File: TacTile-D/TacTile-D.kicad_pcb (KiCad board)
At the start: 2 copper layers, 59.9 x 59.9 mm, 19 parts, among them J1 Conn_01x06, J2 Conn_01x06, J3 Conn_01x06, J4 Conn_01x06, J5 Conn_01x04, J6 Conn_01x05, J7 Conn_01x02, J8 Conn_01x02, U1 74LVC2G08, U10 74LVC1G373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

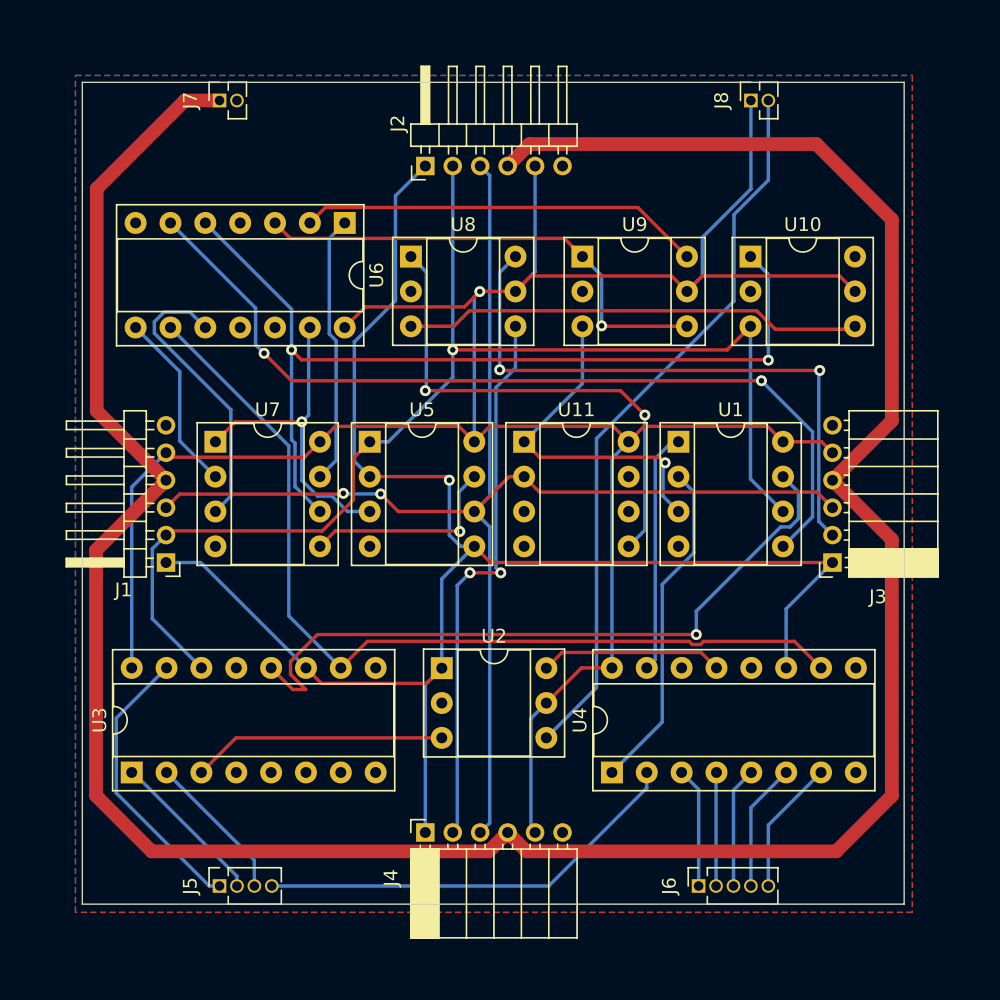
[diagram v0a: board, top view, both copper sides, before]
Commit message: Ensured outputs were disabled on reset - added not gate
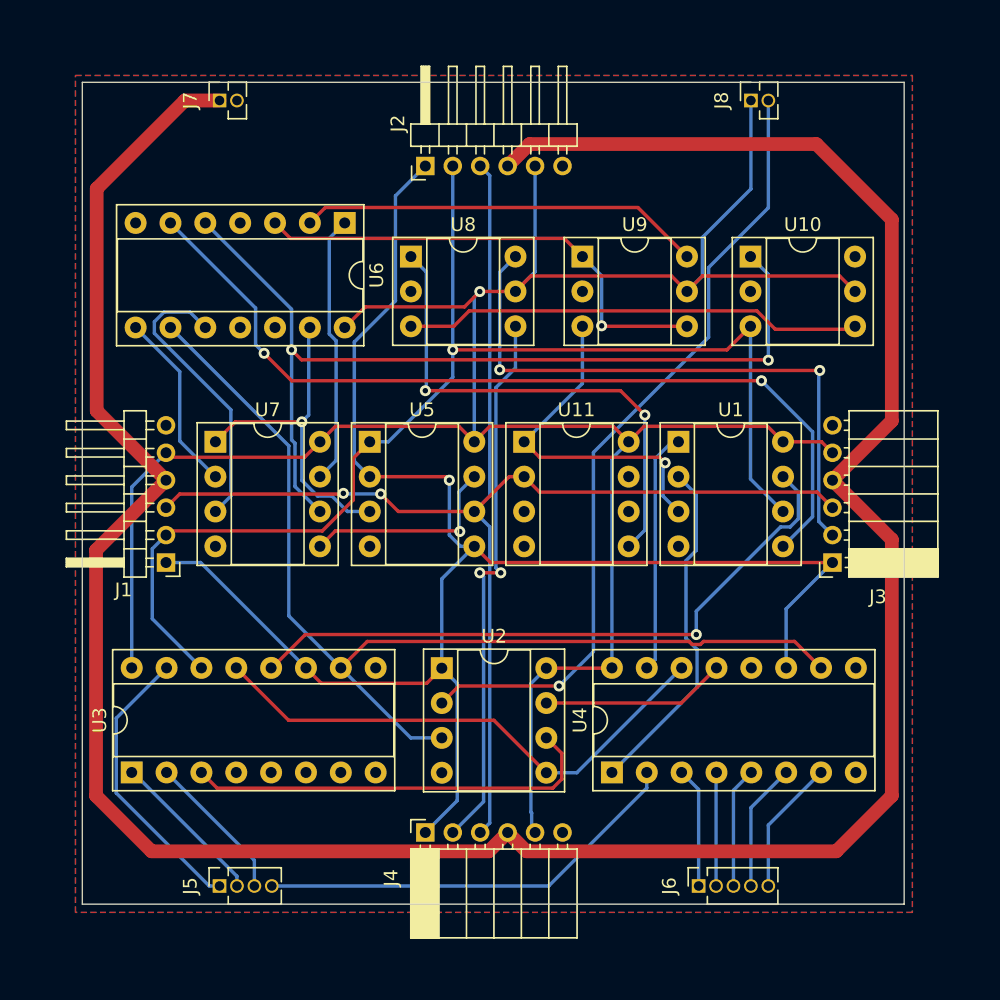
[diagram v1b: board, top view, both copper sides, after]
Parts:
- U2: value 74LVC2G04 -> 74LVC3G04; footprint Package_DIP:DIP-6_W7.62mm_Socket -> Package_DIP:DIP-8_W7.62mm_Socket
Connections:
- U2 pad 2: GND -> LEN
- U2 pad 3: Net-(U3-QD) -> SEN
- U2 pad 4: LEN -> GND
- U2 pad 5: VCC -> Net-(U3-~{OE})
- U2 pad 6: Net-(U4-CPR) -> Net-(U3-QD)
- U3 pad 13: GND -> Net-(U3-~{OE})
- U4 pad 14: GND -> Net-(U3-~{OE})
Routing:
- net Net-(U3-~{OE}): track 0.00 -> 38.8 mm
- net Net-(U3-QD): track 18.6 -> 30.5 mm
- net SEN: track 66.7 -> 76.2 mm
- net LEN: track 53.2 -> 58.1 mm, vias 0 -> 1
- net Net-(U3-RCLK): track 51.5 -> 47.5 mm
- net VCC: track 178.7 -> 180.2 mm
- net CLK: track 119.5 -> 120.5 mm
- net Net-(U4-Q1): track 24.5 -> 25.3 mm

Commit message: Mounted ICs without sockets to save space
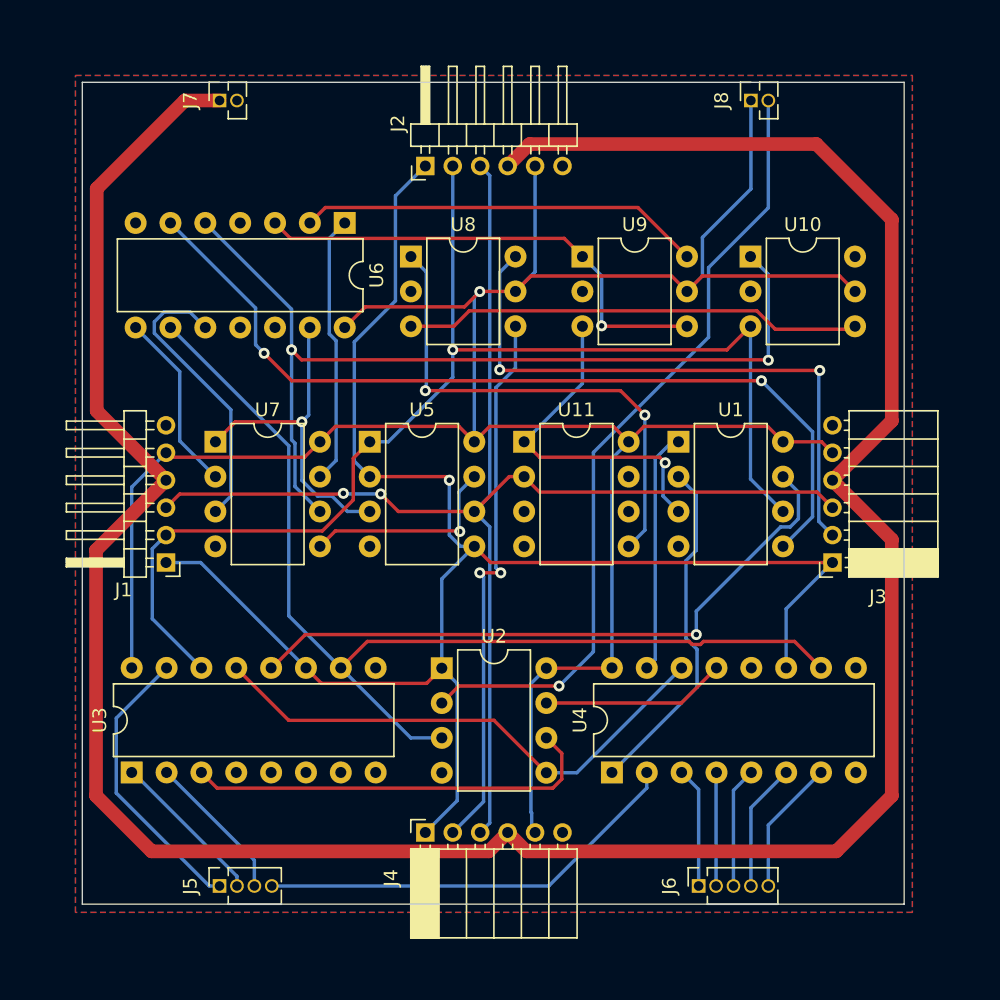
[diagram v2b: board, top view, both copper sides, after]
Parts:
- U1, U11, U2, U5, U7: footprint Package_DIP:DIP-8_W7.62mm_Socket -> Package_DIP:DIP-8_W7.62mm
- U10, U8, U9: footprint Package_DIP:DIP-6_W7.62mm_Socket -> Package_DIP:DIP-6_W7.62mm
- U3, U4: footprint Package_DIP:DIP-16_W7.62mm_Socket -> Package_DIP:DIP-16_W7.62mm
- U6: footprint Package_DIP:DIP-14_W7.62mm_Socket -> Package_DIP:DIP-14_W7.62mm

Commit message: Added photoresistor footprint and enlarged main boards to 60mm
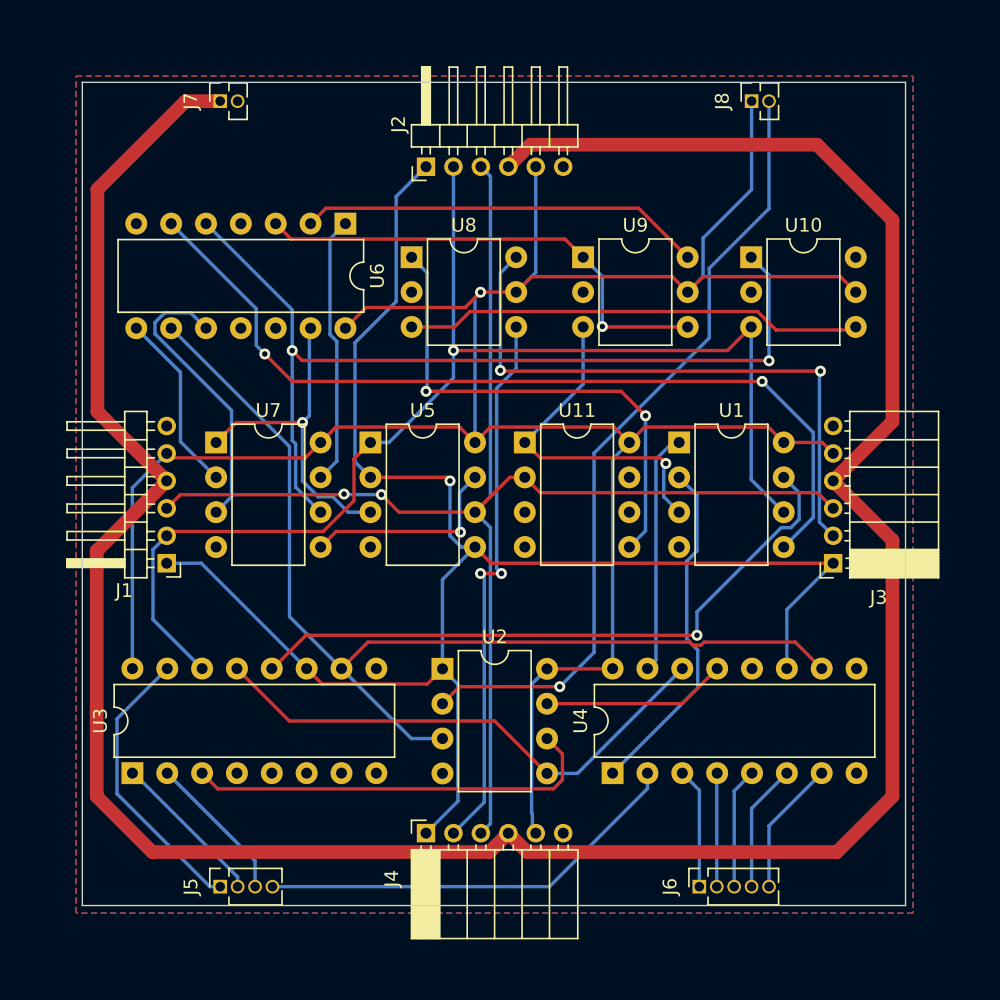
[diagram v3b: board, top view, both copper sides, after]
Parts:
- moved J7 0.07 mm to (35.0, 26.4)
- moved J8 0.07 mm to (73.8, 26.4)
- moved J1 0.07 mm to (31.1, 60.0)
- moved J2 0.07 mm to (50.0, 31.1)
- moved J3 0.07 mm to (79.7, 60.0)
- moved J4 0.07 mm to (50.0, 79.7)
- moved J5 0.07 mm to (35.0, 83.6)
- moved J6 0.07 mm to (70.0, 83.6)
- moved U1 0.07 mm to (68.5, 51.2)
- moved U10 0.07 mm to (73.8, 37.8)
- moved U11 0.07 mm to (57.2, 51.2)
- moved U2 0.07 mm to (51.2, 67.8)
- moved U3 0.07 mm to (28.6, 75.3)
- moved U4 0.07 mm to (63.6, 75.3)
- moved U5 0.07 mm to (46.0, 51.2)
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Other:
- board size 59.9 x 59.9 mm -> 60 x 60 mm

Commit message: Enlarged connectors on board D to 2.54mm pitch
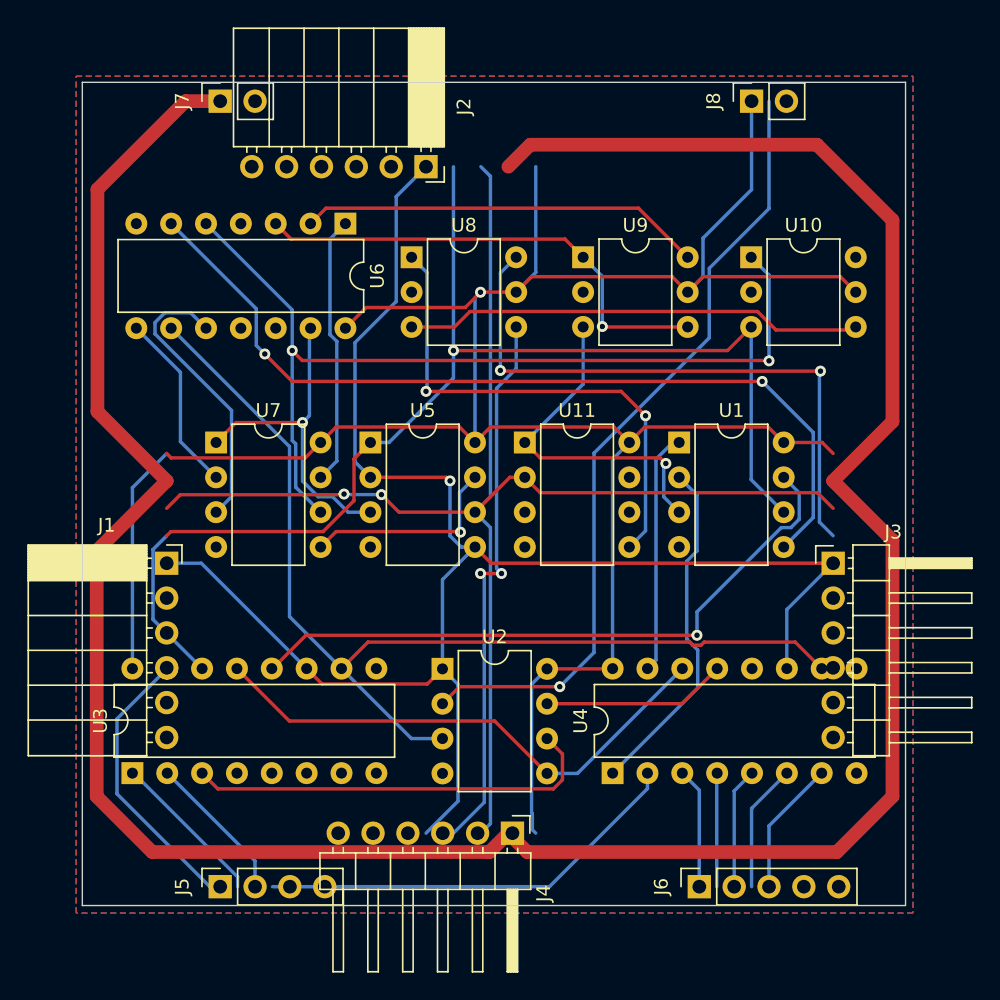
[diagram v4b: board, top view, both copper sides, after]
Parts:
- J1, J2: footprint Connector_PinHeader_2.00mm:PinHeader_1x06_P2.00mm_Horizontal -> Connector_PinSocket_2.54mm:PinSocket_1x06_P2.54mm_Horizontal
- J3, J4: footprint Connector_PinSocket_2.00mm:PinSocket_1x06_P2.00mm_Horizontal -> Connector_PinHeader_2.54mm:PinHeader_1x06_P2.54mm_Horizontal
- J5: footprint Connector_PinSocket_1.27mm:PinSocket_1x04_P1.27mm_Vertical -> Connector_PinSocket_2.54mm:PinSocket_1x04_P2.54mm_Vertical
- J6: footprint Connector_PinSocket_1.27mm:PinSocket_1x05_P1.27mm_Vertical -> Connector_PinSocket_2.54mm:PinSocket_1x05_P2.54mm_Vertical
- J7, J8: footprint Connector_PinSocket_1.27mm:PinSocket_1x02_P1.27mm_Vertical -> Connector_PinSocket_2.54mm:PinSocket_1x02_P2.54mm_Vertical
- moved J4 6.30 mm to (56.4, 79.7), turned to -90 degrees
- turned J1 to 0 degrees
- turned J2 to -90 degrees
- turned J3 to 0 degrees
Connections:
- J1 pad 1: CLK -> GND
- J1 pad 2: MOSI -> VCC
- J1 pad 3: SS -> VIN
- J1 pad 4: VIN -> SS
- J1 pad 5: VCC -> MOSI
- J1 pad 6: GND -> CLK
- J2 pad 1: CLK -> GND
- J2 pad 2: MOSI -> VCC
- J2 pad 3: SS -> VIN
- J2 pad 4: VIN -> SS
- J2 pad 5: VCC -> MOSI
- J2 pad 6: GND -> CLK
- J3 pad 1: CLK -> GND
- J3 pad 2: MISO0 -> VCC
- J3 pad 3: SS -> VIN
- J3 pad 4: VIN -> SS
- J3 pad 5: VCC -> MISO0
- J3 pad 6: GND -> CLK
- J4 pad 1: CLK -> GND
- J4 pad 2: MISO1 -> VCC
- J4 pad 3: SS -> VIN
- J4 pad 4: VIN -> SS
- J4 pad 5: VCC -> MISO1
- J4 pad 6: GND -> CLK

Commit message: Finished rewiring board D
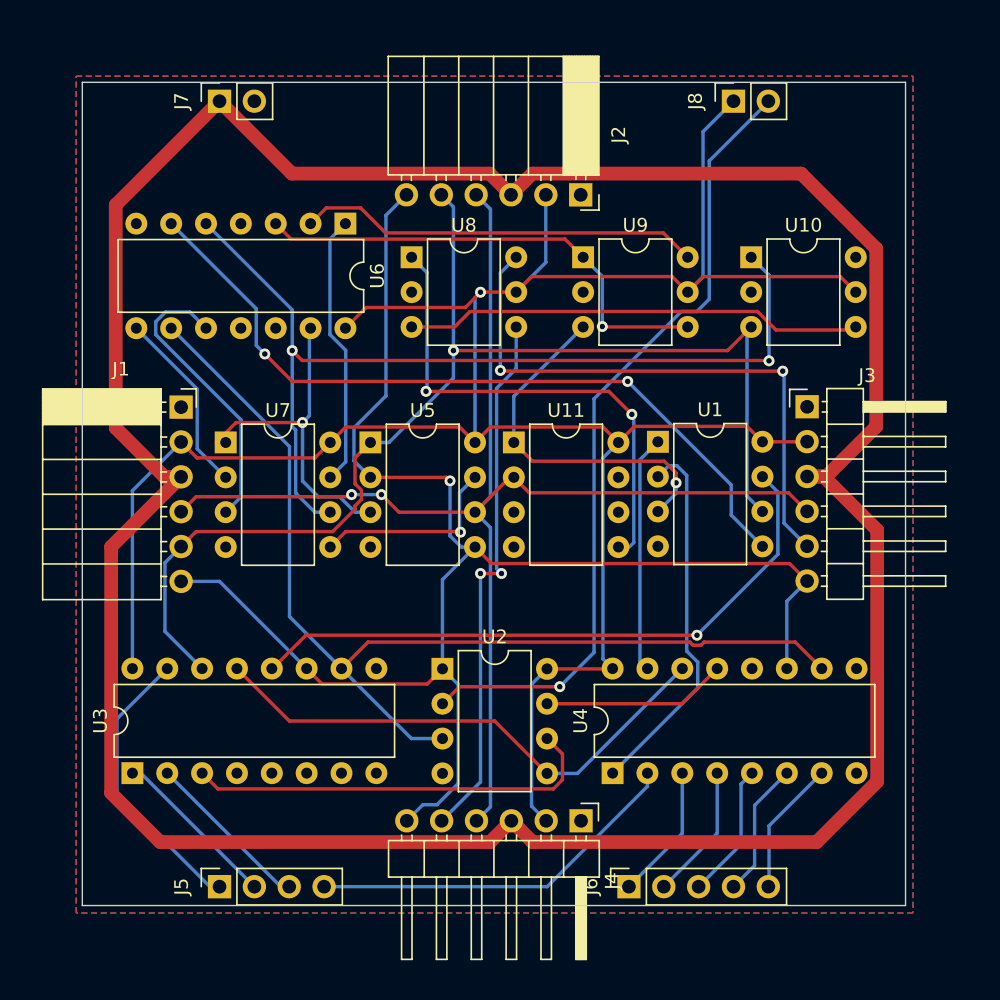
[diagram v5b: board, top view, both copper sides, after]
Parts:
- moved J3 11.6 mm to (77.8, 48.6)
- moved J2 11.5 mm to (61.3, 33.2)
- moved J1 11.4 mm to (32.2, 48.7)
- moved J6 5.13 mm to (64.8, 83.6)
- moved J4 5.08 mm to (61.4, 78.8)
- moved U1 1.55 mm to (67.0, 51.2)
- moved J8 1.32 mm to (72.5, 26.4)
- moved U11 0.80 mm to (56.5, 51.2)
- moved U7 0.70 mm to (35.5, 51.2)
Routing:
- net VIN: track 199.2 -> 216.9 mm
- net Net-(U6A-~{Q}): track 63.9 -> 55.7 mm
- net CLK: track 120.5 -> 113.1 mm
- net SS: track 101.6 -> 96.2 mm
- net VCC: track 180.2 -> 175.9 mm
- net LS3: track 31.4 -> 27.6 mm
- net MOSI: track 92.0 -> 88.8 mm
- net Net-(U4-Q1): track 25.3 -> 27.3 mm
- net MISO0: track 44.5 -> 42.8 mm
- net LS5: track 8.29 -> 9.89 mm
- net Net-(U11-C): track 25.2 -> 26.6 mm
- net LS2: track 10.9 -> 12.3 mm
- net Net-(U11-Q): track 37.1 -> 35.8 mm
- net LS4: track 8.79 -> 9.89 mm
- net LS6: track 8.81 -> 9.89 mm
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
